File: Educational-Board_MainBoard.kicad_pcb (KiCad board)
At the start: 2 copper layers, 200 x 75 mm, 189 parts, among them J201 Screw_Terminal_01x02_P5mm, J202 USB-C_304A-ACP16X, J401 ACC_INT1, J402 BME_SPI, J403 LUX_INT, J501 RGB_OUT, J601 PWR_IN1, J602 PWR_IN2, J603 PWR_IN3, J604 PWR_IN4, J605 MCP_INT, J606 5V, J607 GND, J608 3V3, J609 EX_PA, J610 EX_PB, J611 PWR_OUT1, J612 PWR_OUT3, J613 PWR_OUT2, J614 PWR_OUT4, Q501 AO3400A, Q601 IRLML9301TRPBF, Q602 IRLML9301TRPBF, Q603 IRLML9301TRPBF, Q604 IRLML9301TRPBF, SW301 RESET, SW501 BUTTON1, SW502 BUTTON2, SW503 BUTTON3, SW504 BUTTON4, SW505 BUTTON5, U201 TPS5430DDA, U202 NUCLEO64-H503RB, U401 LSM6DS3, U402 BME280, U403 OPT4001, U404 INA2180A2, U406 YK16S-L7.2-B10Ka(32-8)-G-A29, U501 74LVC1G34, U502 SSD1315 OLED 0.98", U601 TLP291-4, U602 TLP291-4, U603 MCP23017_SS

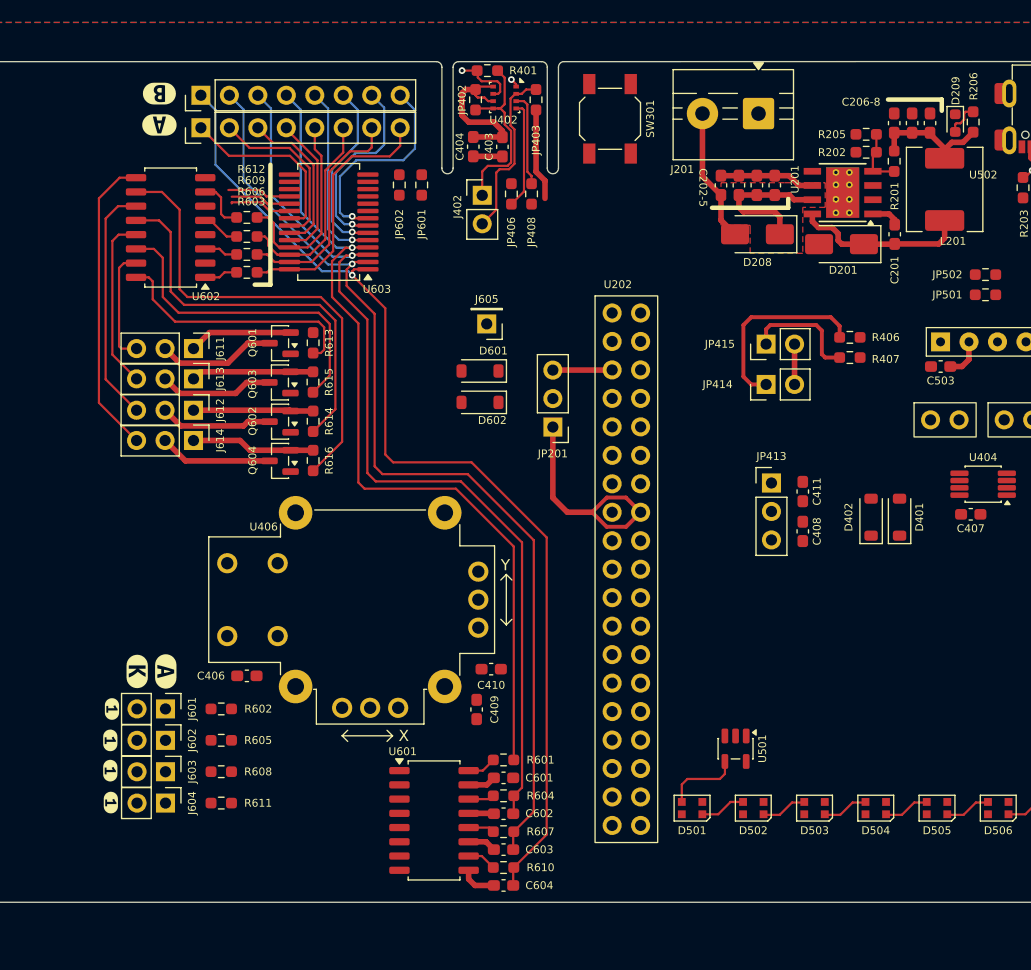
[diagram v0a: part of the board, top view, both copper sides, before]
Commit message: Routed the another part of POWER_UI
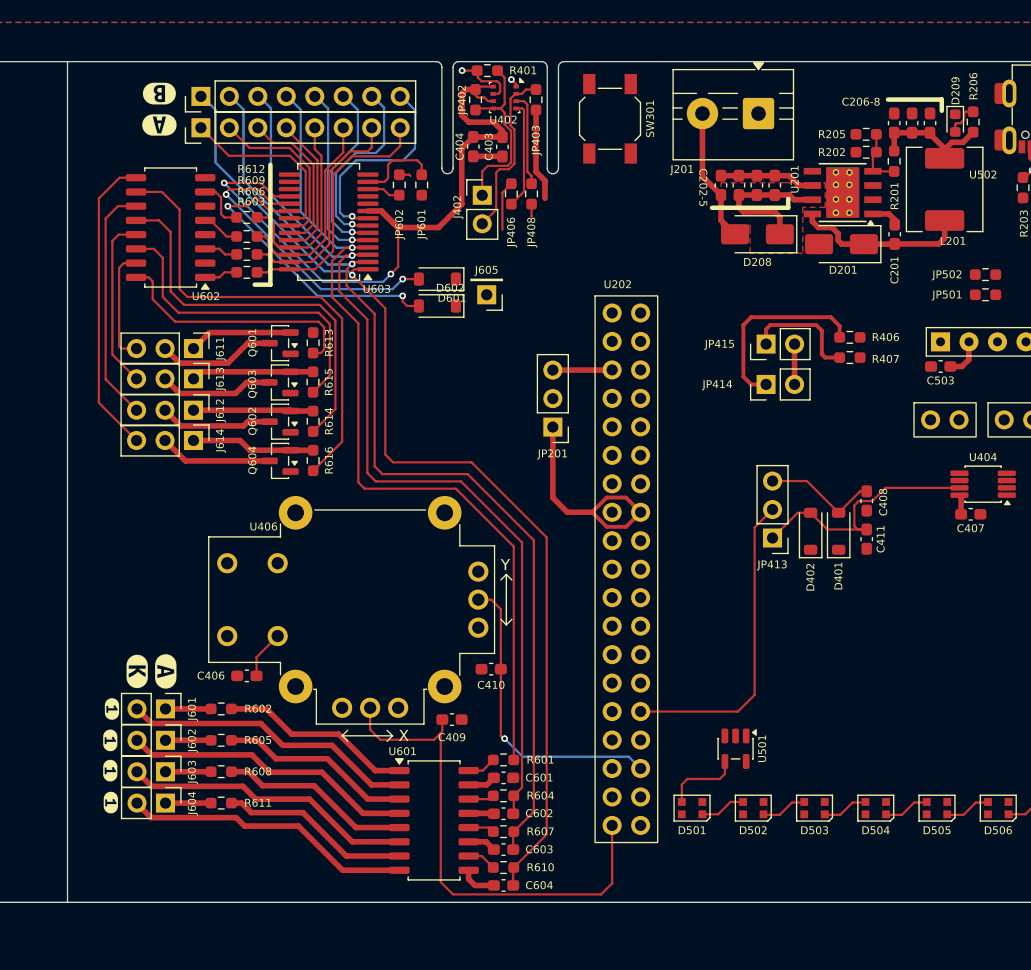
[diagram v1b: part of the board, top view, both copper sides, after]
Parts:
- moved D602 9.40 mm to (103.0, 71.8)
- moved D601 9.04 mm to (103.0, 69.4)
- moved C411 7.11 mm to (141.3, 92.6)
- moved C408 6.31 mm to (141.3, 89.2), turned to -90 degrees
- moved D401 5.58 mm to (138.8, 91.9)
- moved D402 5.54 mm to (136.3, 91.9)
- moved JP413 4.91 mm to (132.9, 92.5), turned to 180 degrees
- moved J605 2.60 mm to (107.4, 70.8)
- moved C409 2.38 mm to (104.3, 108.7), turned to 0 degrees
- moved J610 0.10 mm to (81.9, 53.1)
- turned R608 to 0 degrees
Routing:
- net +3V3: track 48.0 -> 93.1 mm, vias 0 -> 2
- net /MCU/JOYSTICK_X: track 0.00 -> 44.8 mm
- net /MCU/I_SENSE: track 0.00 -> 28.0 mm
- net /MCU/JOYSTICK_Y: track 0.00 -> 27.3 mm, vias 0 -> 1
- net Net-(J601-Pin_2): track 0.00 -> 26.2 mm
- net Net-(J602-Pin_2): track 0.00 -> 26.1 mm
- net Net-(J603-Pin_2): track 0.00 -> 26.0 mm
- net Net-(J604-Pin_2): track 0.00 -> 26.0 mm
- net Net-(D402-A): track 0.00 -> 23.0 mm
- net /POWER_UI/INT_A: track 5.41 -> 27.6 mm, vias 0 -> 2
- net /POWER_UI/INT_B: track 5.57 -> 27.5 mm, vias 0 -> 2
- net Net-(R602-Pad2): track 0.00 -> 17.3 mm
- net Net-(R605-Pad2): track 0.00 -> 17.2 mm
- net Net-(R608-Pad2): track 0.00 -> 17.0 mm
- net Net-(R611-Pad2): track 0.00 -> 16.9 mm
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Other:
- outline, holes or cut-outs redrawn

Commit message: Continued routing + resized the board
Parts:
- added H101: MountingHole, MountingHole:MountingHole_3.2mm_M3_ISO14580, F.Cu at (73.0, 53.5)
- added H102: MountingHole, MountingHole:MountingHole_3.2mm_M3_ISO14580, F.Cu at (236.0, 53.5)
- added H103: MountingHole, MountingHole:MountingHole_3.2mm_M3_ISO14580, F.Cu at (236.0, 121.5)
- added H104: MountingHole, MountingHole:MountingHole_3.2mm_M3_ISO14580, F.Cu at (73.0, 121.5)
- moved R303 53.7 mm to (173.6, 86.0), turned to 0 degrees
- moved D301 53.2 mm to (173.6, 84.2), turned to 0 degrees
- moved kibuzzard-69F29536 3.37 mm to (70.6, 107.8)
- moved kibuzzard-69F29536 3.27 mm to (70.6, 116.1)
- moved kibuzzard-69F29536 3.22 mm to (70.6, 113.4)
- moved kibuzzard-69F29536 3.22 mm to (70.6, 110.6)
- moved JP502 2.97 mm to (154.0, 71.1), turned to 180 degrees
- moved JP412 2.91 mm to (167.7, 81.0), turned to 90 degrees
- moved kibuzzard-69F2951E 2.82 mm to (73.4, 104.2)
- moved J601 2.80 mm to (75.9, 107.8)
- moved J602 2.80 mm to (75.9, 110.5)
- moved J603 2.80 mm to (75.9, 113.4)
- moved J604 2.80 mm to (75.9, 116.2)
- moved kibuzzard-69F28E96 2.77 mm to (76.0, 104.2)
- moved JP411 2.62 mm to (167.7, 78.2), turned to 90 degrees
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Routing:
- net +3V3: track 93.1 -> 279.4 mm
- net /MCU/JOYSTICK_BTN: track 4.33 -> 128.2 mm, vias 0 -> 2
- net /Power/OUT_BUCK: track 11.6 -> 113.2 mm
- net +5V: track 0.00 -> 94.6 mm
- net /Sensors/SHUNT_VDD: track 3.60 -> 73.1 mm
- net /MCU/BUZZER_TIM2: track 0.00 -> 64.8 mm, vias 0 -> 2
- net /Sensors/SHUNT_3V3: track 0.00 -> 27.7 mm
- net /MCU/WS2812_PWM: track 0.00 -> 24.8 mm
- net GND: track 42.7 -> 66.5 mm, vias 3 -> 6
- net /UI/BUZZER: track 0.00 -> 23.5 mm
- net /Sensors/SHUNT_MCU_VDD: track 0.00 -> 20.5 mm
- net Net-(D401-A): track 10.4 -> 23.8 mm, vias 0 -> 2
- net /MCU/WS2812_SPI: track 0.00 -> 9.26 mm
- net /MCU/LED2: track 0.00 -> 8.99 mm, vias 0 -> 1
- net /MCU/I2C1_SCL: track 0.00 -> 8.59 mm
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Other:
- board size 200 x 75 mm -> 170 x 75 mm

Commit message: Some placing and routing
Added joystick 3D model
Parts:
- added kibuzzard-69F3BF46: G***, kibuzzard-69F3BF46, F.Cu at (122.2, 58.4)
- moved C404 104.4 mm to (210.6, 57.5)
- moved C403 104.4 mm to (213.2, 57.5)
- moved JP402 104.4 mm to (210.8, 53.3)
- moved JP403 104.4 mm to (216.2, 53.3)
- moved JP408 104.4 mm to (215.8, 61.7)
- moved R401 104.4 mm to (211.9, 50.7)
- moved U402 104.4 mm to (213.4, 53.1)
- moved J402 104.4 mm to (211.4, 61.9)
- moved JP406 104.4 mm to (214.0, 61.7)
- moved C406 98.4 mm to (184.4, 106.3), turned to -90 degrees
- moved J605 95.0 mm to (20.3, 108.7), turned to 0 degrees
- moved D601 88.2 mm to (24.7, 110.1), turned to 0 degrees
- moved D602 86.1 mm to (24.7, 107.7), turned to 0 degrees
- moved C506 75.5 mm to (123.8, 97.3), turned to 90 degrees
- moved R512 74.5 mm to (123.8, 100.7)
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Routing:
- net /MCU/JOYSTICK_BTN: track 128.2 -> 2.31 mm, vias 2 -> 0
- net /MCU/I2C_SCL: track 9.40 -> 133.9 mm
- net +3V3: track 279.4 -> 156.1 mm, vias 2 -> 4
- net /MCU/I2C_SDA: track 8.46 -> 129.9 mm, vias 0 -> 6
- net /POWER_UI/PB0: track 92.2 -> 3.31 mm, vias 3 -> 0
- net /POWER_UI/PB1: track 87.6 -> 6.03 mm, vias 3 -> 0
- net /POWER_UI/PB2: track 83.7 -> 7.68 mm, vias 3 -> 0
- net /UI/RGB_DIN: track 6.90 -> 80.6 mm, vias 0 -> 2
- net /POWER_UI/PB3: track 77.9 -> 9.92 mm, vias 3 -> 0
- net /MCU/BUZZER_TIM2: track 64.8 -> 2.66 mm, vias 2 -> 0
- net /Power/OUT_BUCK: track 113.2 -> 54.6 mm, vias 0 -> 2
- net /MCU/JOYSTICK_X: track 45.9 -> 2.32 mm
- net /MCU/RESETn: track 0.00 -> 38.4 mm, vias 0 -> 1
- net +5V: track 94.6 -> 126.7 mm, vias 0 -> 2
- net /POWER_UI/BJT4_C: track 41.9 -> 10.0 mm
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- added copper zone on F.Cu, net /Power/OUT_BUCK
- added copper zone on F.Cu, net /Power/PH_BUCK
- added copper zone on F.Cu, net /Power/VIN
- added copper zone on F.Cu, net /Power/VUSB
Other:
- board size 170 x 75 mm -> 170 x 75.1 mm

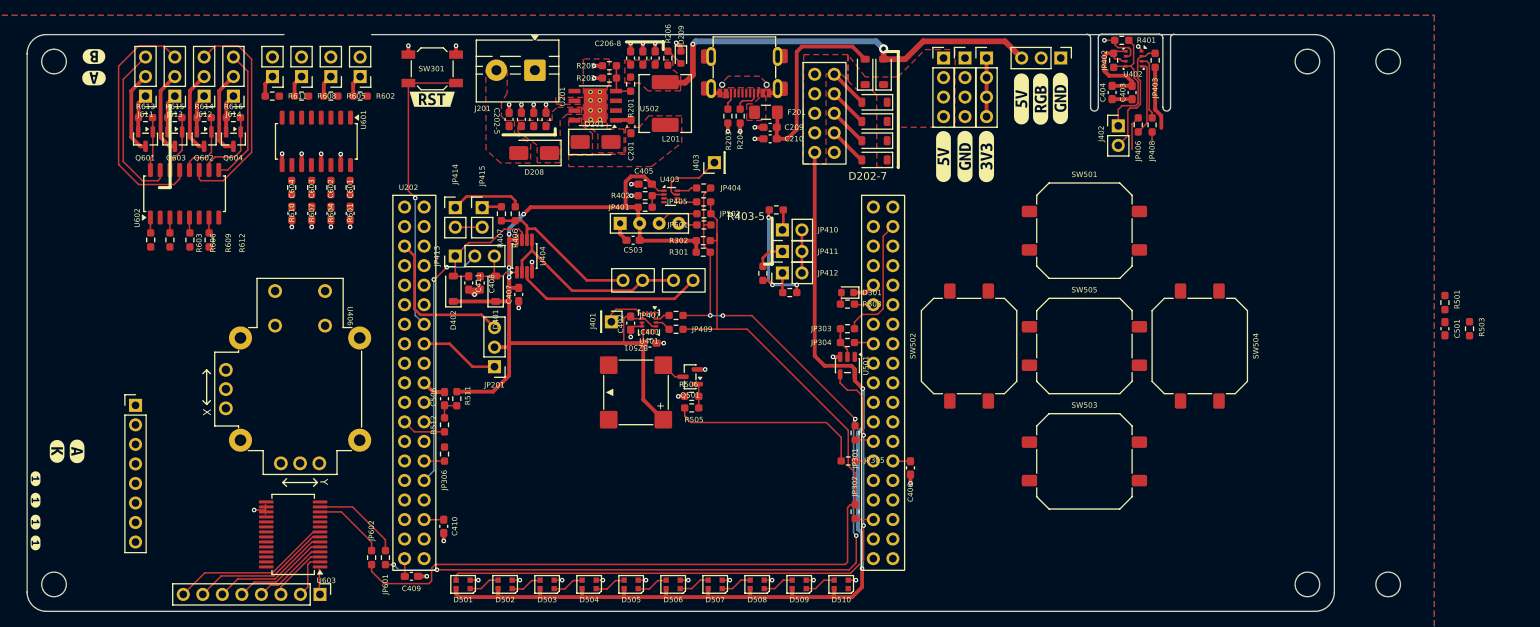
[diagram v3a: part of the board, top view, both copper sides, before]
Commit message: fixed i2c swap bridge (to be checked if now are ok) routed bme280
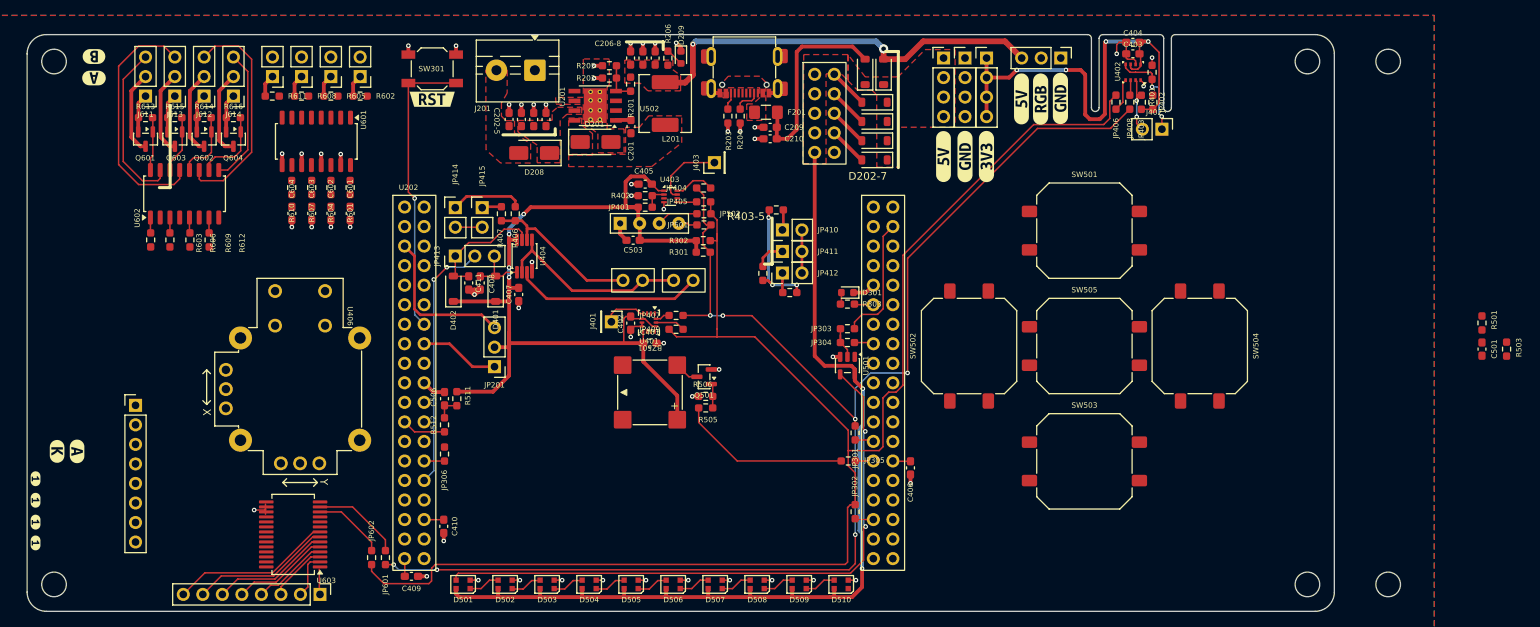
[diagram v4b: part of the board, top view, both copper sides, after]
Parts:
- moved JP402 7.47 mm to (215.9, 58.8), turned to -90 degrees
- moved C404 7.07 mm to (213.3, 51.0), turned to 180 degrees
- moved JP403 5.74 mm to (214.4, 58.8)
- moved R401 5.73 mm to (215.8, 54.9), turned to 90 degrees
- moved J402 5.69 mm to (217.1, 62.3), turned to -90 degrees
- moved C501 5.50 mm to (258.7, 90.9)
- moved R501 5.50 mm to (258.7, 87.5)
- moved R503 5.50 mm to (261.9, 90.9)
- moved C403 5.04 mm to (213.3, 52.5), turned to 180 degrees
- moved JP406 4.14 mm to (211.1, 58.8)
- moved JP408 4.14 mm to (212.9, 58.8)
- moved BZ501 1.82 mm to (150.5, 96.5)
- moved Q501 1.82 mm to (157.5, 94.5)
- moved R505 1.82 mm to (157.7, 98.5)
- moved R506 1.82 mm to (157.7, 97.0)
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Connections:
- U202 pad 18: unconnected-(U202A-+5V-Pad18) -> +5V
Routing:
- net /MCU/I2C_SCL: track 133.9 -> 201.1 mm
- net /MCU/I2C_SDA: track 129.9 -> 192.2 mm, vias 6 -> 7
- net +3V3: track 156.1 -> 188.3 mm, vias 4 -> 8
- net Net-(J402-Pin_2): track 15.6 -> 8.05 mm, vias 0 -> 2
- net Net-(JP408-A): track 8.35 -> 2.00 mm
- net Net-(JP406-A): track 9.62 -> 4.30 mm
- net Net-(J402-Pin_1): track 16.3 -> 12.4 mm, vias 0 -> 2
- net /UI/BUZZER: track 25.6 -> 22.5 mm
- net Net-(JP404-A): track 2.67 -> 5.28 mm
- net Net-(JP409-A): track 2.06 -> 3.89 mm
- net Net-(J403-Pin_1): track 8.78 -> 9.49 mm
- net GND: track 78.9 -> 79.2 mm, vias 50 -> 52
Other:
- board size 170 x 75.1 mm -> 170 x 75 mm

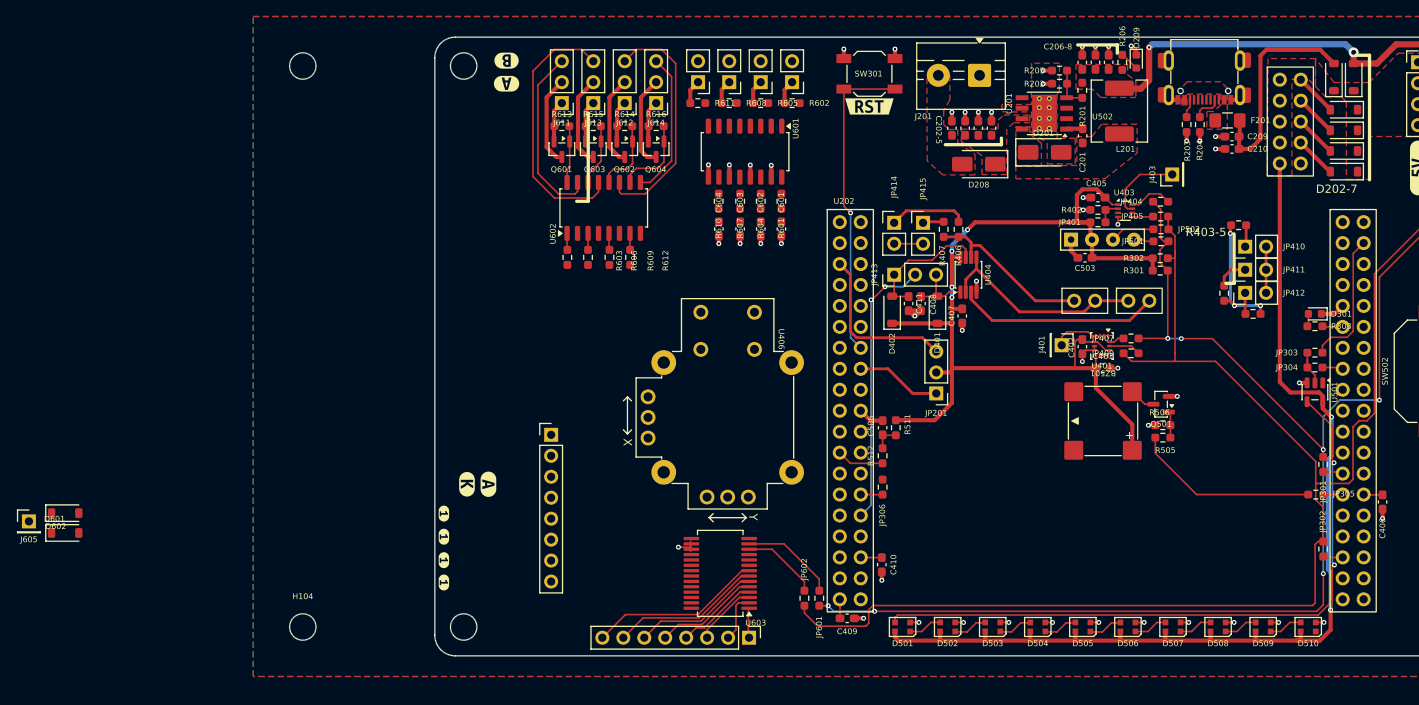
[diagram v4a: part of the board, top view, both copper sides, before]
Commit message: Continuated routing + fixing SSD1306 footprint
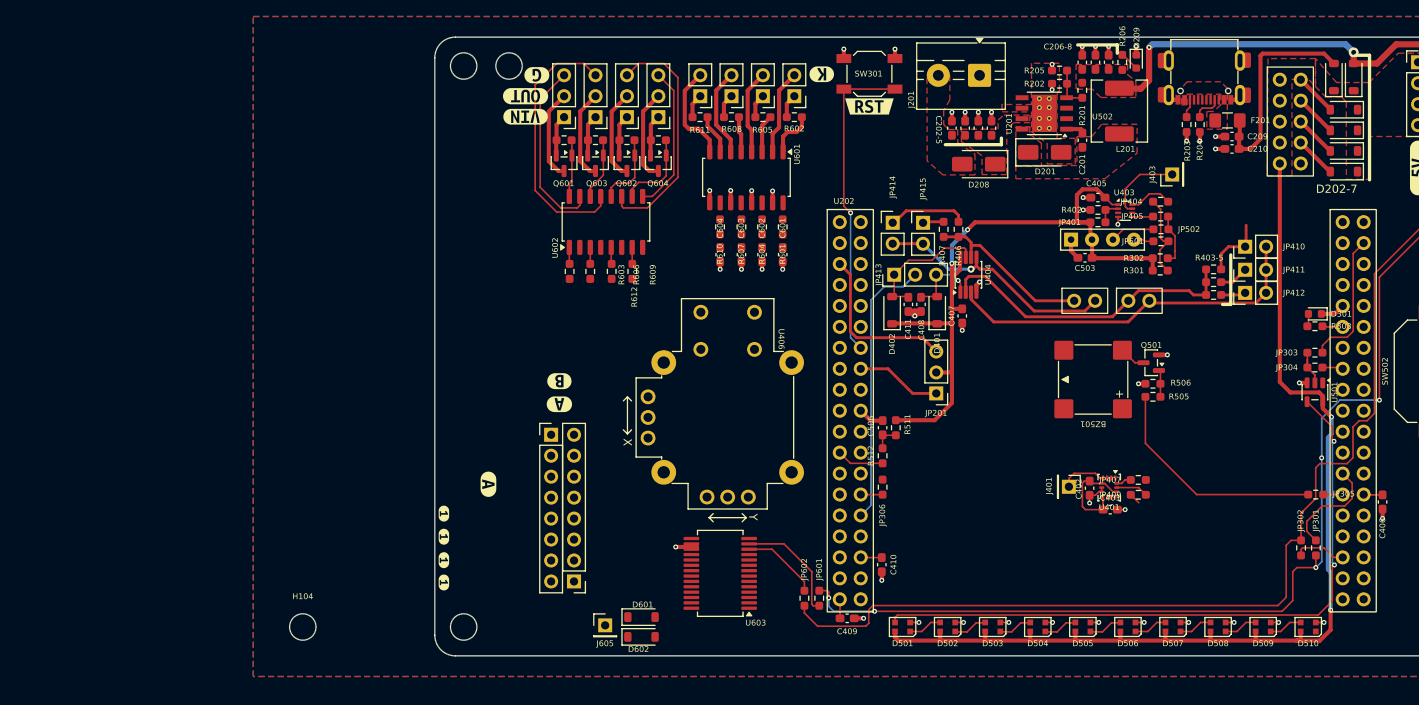
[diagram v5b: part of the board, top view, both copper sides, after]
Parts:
- added kibuzzard-69F9CDB6: G***, kibuzzard-69F9CDB6, F.Cu at (81.9, 54.6)
- added kibuzzard-69F9D252: G***, kibuzzard-69F9D252, F.Cu at (80.5, 57.2)
- added kibuzzard-69F9D27B: G***, kibuzzard-69F9D27B, F.Cu at (80.5, 59.7)
- moved J605 71.0 mm to (90.2, 121.3)
- moved D601 71.0 mm to (94.5, 122.7)
- moved D602 71.0 mm to (94.5, 120.3)
- moved kibuzzard-69F2951E 65.7 mm to (116.4, 54.5), turned to 180 degrees
- moved kibuzzard-69F28E96 39.4 mm to (84.6, 94.5)
- moved kibuzzard-69F28EB1 39.4 mm to (84.6, 91.7)
- moved H101 25.0 mm to (78.5, 53.5)
- moved J610 22.3 mm to (86.4, 116.0), turned to 180 degrees
- moved C401 17.2 mm to (151.4, 107.3)
- moved C402 17.2 mm to (148.9, 104.7)
- moved JP407 17.2 mm to (154.8, 103.7)
- moved JP409 17.2 mm to (154.8, 105.5)
- moved U401 17.2 mm to (151.2, 104.6)
- moved J401 17.2 mm to (146.4, 104.5)
- moved JP301 10.2 mm to (176.3, 111.9), turned to -90 degrees
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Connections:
- JP414 pad 2: /Sensors/SHUNT_VDD -> /Sensors/SHUNT_VDD2
- JP415 pad 2: /Sensors/SHUNT_VDD -> /Sensors/SHUNT_VDD2
- U202 pad 78: /Sensors/SHUNT_VDD -> /Sensors/SHUNT_VDD2
- U404 pad 5: /Sensors/SHUNT_VDD -> /Sensors/SHUNT_VDD2
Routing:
- net /MCU/I2C_SCL: track 201.1 -> 154.4 mm
- net /MCU/I2C_SDA: track 192.2 -> 156.4 mm, vias 7 -> 5
- net /Sensors/SHUNT_VDD2: track 0.00 -> 29.8 mm, vias 0 -> 1
- net +3V3: track 188.3 -> 158.6 mm, vias 8 -> 6
- net /POWER_UI/PB7: track 21.2 -> 0.00 mm
- net /POWER_UI/PB6: track 18.3 -> 0.00 mm
- net /POWER_UI/PB5: track 15.5 -> 0.00 mm
- net /Sensors/SHUNT_3V3: track 30.1 -> 45.0 mm
- net /POWER_UI/PB4: track 12.7 -> 0.00 mm
- net Net-(J604-Pin_2): track 0.00 -> 12.1 mm
- net Net-(J603-Pin_2): track 0.00 -> 10.8 mm
- net /MCU/I2C1_SDA: track 2.45 -> 12.9 mm
- net Net-(J601-Pin_2): track 0.00 -> 10.4 mm
- net Net-(J602-Pin_2): track 0.00 -> 10.3 mm
- net /POWER_UI/PB3: track 9.92 -> 0.00 mm
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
